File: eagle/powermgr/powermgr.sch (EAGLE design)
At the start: 18 parts, among them IC1 PIC16F1455, IC2 4027D, IC3 MCP1703DB, Q1 BSS123, Q2 BSS123, X1 MINI-USB-32005-201

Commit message: First pass of power management board completed
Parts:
- added C10, C9: .1u, resistor:C-EUC0603K
- added C11, C8: 10n, resistor:C-EUC0603K
- added C7: 0.1u, resistor:C-USC1206K
- added IC4: ACS756, custom:ACS756
- added JP5: (no value), pinhead:PINHD-1X2
- added JP6: (no value), pinhead:PINHD-1X6
- added R3: 1k, resistor:R-US_R0603
- added R4: 50k, resistor:R-US_R0603
- added R5, R6: 10k, resistor:R-US_R0603
- added R7: 220, resistor:R-US_R0603
- added X2: (no value), con-wago-500:W237-4
- C3: value (none) -> 47u; device resistor:C-EUC0805 -> resistor:CPOL-USE2.5-6
- C4, C5: value (none) -> .1u
- C6: value (none) -> 1u
- IC1: value PIC16F1455 -> PIC16F1455TSSOP-14; device custom:PIC16F1455 -> custom:PIC16F1455TSSOP-14
- IC3: value MCP1703DB -> MCP1804
- X1: value MINI-USB-32005-201 -> 10104111-0001LF; device con-cypressindustries:MINI-USB-32005-201 -> custom:10104111-0001LF
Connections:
- new net CURRENT: C8.1, IC1.RC3, R3.2
- new net N$10: C11.1, IC1.RC2, R4.1, R5.2
- new net N$11: JP6.1, R6.2, R7.2
- new net N$5: IC4.IP+, X2-1.KL, X2-2.KL
- new net N$6: IC4.IP-, X2-3.KL, X2-4.KL
- new net N$9: IC4.VOUT, R3.1
- net !MCLR: now also R7.1
- net +24V: now also C3.+, JP5.1, R4.2; no longer C3.2
- net +5V: now also C10.2, C7.1, C9.1, IC4.VCC, JP6.2, R6.1; no longer X1.1
- net GND: now also C10.1, C11.2, C3.-, C7.2, C8.2, C9.2, IC4.GND, JP5.2, JP6.3, R5.1, X1.GND; no longer C3.1, X1.5
- net ICSPCLK: now also JP6.5
- net ICSPDAT: now also JP6.4
- net USBD+: now also X1.D+; no longer X1.3
- net USBD-: now also X1.D-; no longer X1.2
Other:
- moved on the sheet: C4, C5, C6, IC3

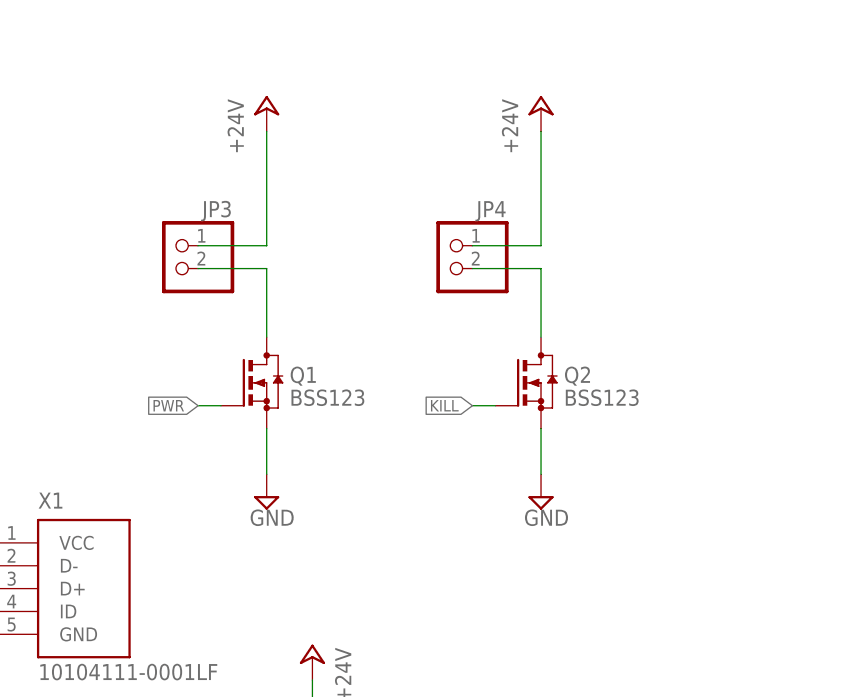
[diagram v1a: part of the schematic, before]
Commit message: Added LEDs, finalized silkscreen
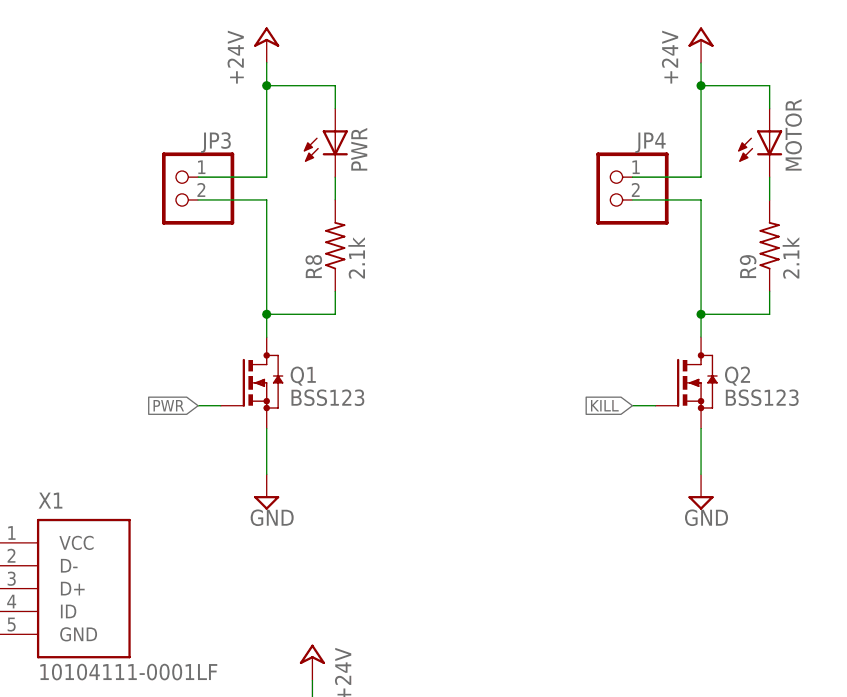
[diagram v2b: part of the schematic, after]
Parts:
- added MOTOR, PWR: (no value), led:LEDCHIP-LED0805
- added R8, R9: 2.1k, resistor:R-US_R0805
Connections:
- new net N$12: MOTOR.C, R9.2
- new net N$7: PWR.C, R8.2
- net +24V: now also MOTOR.A, PWR.A
- net N$3: now also R8.1
- net N$4: now also R9.1
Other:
- moved on the sheet: JP3, JP4, Q2
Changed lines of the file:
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@@
 <part name="SUPPLY11" library="supply2" deviceset="GND" device=""/>
 <part name="C11" library="resistor" deviceset="C-EU" device="C0603K" value="10n"/>
+<part name="R8" library="resistor" deviceset="R-US_" device="R0805" value="2.1k"/>
+<part name="R9" library="resistor" deviceset="R-US_" device="R0805" value="2.1k"/>
+<part name="PWR" library="led" deviceset="LED" device="CHIP-LED0805"/>
+<part name="MOTOR" library="led" deviceset="LED" device="CHIP-LED0805"/>
 </parts>
 <sheets>
@@
 <instance part="C2" gate="G$1" x="-86.36" y="27.94"/>
 <instance part="Q1" gate="G$1" x="134.62" y="78.74"/>
-<instance part="Q2" gate="G$1" x="165.1" y="78.74"/>
-<instance part="JP3" gate="G$1" x="124.46" y="91.44" rot="MR0"/>
-<instance part="JP4" gate="G$1" x="154.94" y="91.44" rot="MR0"/>
+<instance part="Q2" gate="G$1" x="182.88" y="78.74"/>
+<instance part="JP3" gate="G$1" x="124.46" y="99.06" rot="MR0"/>
+<instance part="JP4" gate="G$1" x="172.72" y="99.06" rot="MR0"/>
 <instance part="SUPPLY4" gate="GND" x="134.62" y="66.04"/>
-<instance part="SUPPLY5" gate="GND" x="165.1" y="66.04"/>
-<instance part="P+4" gate="1" x="134.62" y="109.22"/>
-<instance part="P+5" gate="1" x="165.1" y="109.22"/>
+<instance part="SUPPLY5" gate="GND" x="182.88" y="66.04"/>
+<instance part="P+4" gate="1" x="134.62" y="116.84"/>
+<instance part="P+5" gate="1" x="182.88" y="116.84"/>
 <instance part="SUPPLY6" gate="GND" x="101.6" y="43.18"/>
 <instance part="IC3" gate="G$1" x="71.12" y="106.68"/>
@@
 <instance part="SUPPLY11" gate="GND" x="63.5" y="-25.4"/>
 <instance part="C11" gate="G$1" x="147.32" y="22.86"/>
+<instance part="R8" gate="G$1" x="142.24" y="93.98" rot="R90"/>
+<instance part="R9" gate="G$1" x="190.5" y="93.98" rot="R90"/>
+<instance part="PWR" gate="G$1" x="142.24" y="106.68"/>
+<instance part="MOTOR" gate="G$1" x="190.5" y="106.68"/>
 </instances>
 <busses>
@@
 <pinref part="Q2" gate="G$1" pin="S"/>
 <pinref part="SUPPLY5" gate="GND" pin="GND"/>
-<wire x1="165.1" y1="73.66" x2="165.1" y2="68.58" width="0.1524" layer="91"/>
+<wire x1="182.88" y1="73.66" x2="182.88" y2="68.58" width="0.1524" layer="91"/>
 </segment>
 <segment>
@@
 <segment>
 <pinref part="Q2" gate="G$1" pin="G"/>
-<wire x1="160.02" y1="76.2" x2="157.48" y2="76.2" width="0.1524" layer="91"/>
-<label x="157.48" y="76.2" size="1.27" layer="95" rot="R180" xref="yes"/>
+<wire x1="177.8" y1="76.2" x2="175.26" y2="76.2" width="0.1524" layer="91"/>
+<label x="175.26" y="76.2" size="1.27" layer="95" rot="R180" xref="yes"/>
 </segment>
 </net>
@@
 <pinref part="Q1" gate="G$1" pin="D"/>
 <pinref part="JP3" gate="G$1" pin="2"/>
-<wire x1="134.62" y1="83.82" x2="134.62" y2="91.44" width="0.1524" layer="91"/>
-<wire x1="134.62" y1="91.44" x2="127" y2="91.44" width="0.1524" layer="91"/>
+<wire x1="134.62" y1="83.82" x2="134.62" y2="86.36" width="0.1524" layer="91"/>
+<wire x1="134.62" y1="86.36" x2="134.62" y2="99.06" width="0.1524" layer="91"/>
+<wire x1="134.62" y1="99.06" x2="127" y2="99.06" width="0.1524" layer="91"/>
+<pinref part="R8" gate="G$1" pin="1"/>
+<wire x1="142.24" y1="88.9" x2="142.24" y2="86.36" width="0.1524" layer="91"/>
+<wire x1="142.24" y1="86.36" x2="134.62" y2="86.36" width="0.1524" layer="91"/>
+<junction x="134.62" y="86.36"/>
 </segment>
 </net>
@@
 <pinref part="Q2" gate="G$1" pin="D"/>
 <pinref part="JP4" gate="G$1" pin="2"/>
-<wire x1="165.1" y1="83.82" x2="165.1" y2="91.44" width="0.1524" layer="91"/>
-<wire x1="165.1" y1="91.44" x2="157.48" y2="91.44" width="0.1524" layer="91"/>
+<wire x1="182.88" y1="83.82" x2="182.88" y2="86.36" width="0.1524" layer="91"/>
+<wire x1="182.88" y1="86.36" x2="182.88" y2="99.06" width="0.1524" layer="91"/>
+<wire x1="182.88" y1="99.06" x2="175.26" y2="99.06" width="0.1524" layer="91"/>
+<pinref part="R9" gate="G$1" pin="1"/>
+<wire x1="190.5" y1="88.9" x2="190.5" y2="86.36" width="0.1524" layer="91"/>
+<wire x1="190.5" y1="86.36" x2="182.88" y2="86.36" width="0.1524" layer="91"/>
+<junction x="182.88" y="86.36"/>
 </segment>
 </net>
@@
 <segment>
 <pinref part="JP3" gate="G$1" pin="1"/>
-<wire x1="127" y1="93.98" x2="134.62" y2="93.98" width="0.1524" layer="91"/>
-<wire x1="134.62" y1="93.98" x2="134.62" y2="106.68" width="0.1524" layer="91"/>
+<wire x1="127" y1="101.6" x2="134.62" y2="101.6" width="0.1524" layer="91"/>
+<wire x1="134.62" y1="101.6" x2="134.62" y2="111.76" width="0.1524" layer="91"/>
 <pinref part="P+4" gate="1" pin="+24V"/>
+<wire x1="134.62" y1="111.76" x2="134.62" y2="114.3" width="0.1524" layer="91"/>
+<wire x1="134.62" y1="111.76" x2="142.24" y2="111.76" width="0.1524" layer="91"/>
+<junction x="134.62" y="111.76"/>
+<pinref part="PWR" gate="G$1" pin="A"/>
+<wire x1="142.24" y1="111.76" x2="142.24" y2="109.22" width="0.1524" layer="91"/>
 </segment>
 <segment>
 <pinref part="JP4" gate="G$1" pin="1"/>
-<wire x1="157.48" y1="93.98" x2="165.1" y2="93.98" width="0.1524" layer="91"/>
-<wire x1="165.1" y1="93.98" x2="165.1" y2="106.68" width="0.1524" layer="91"/>
+<wire x1="175.26" y1="101.6" x2="182.88" y2="101.6" width="0.1524" layer="91"/>
+<wire x1="182.88" y1="101.6" x2="182.88" y2="111.76" width="0.1524" layer="91"/>
 <pinref part="P+5" gate="1" pin="+24V"/>
+<wire x1="182.88" y1="111.76" x2="182.88" y2="114.3" width="0.1524" layer="91"/>
+<wire x1="182.88" y1="111.76" x2="190.5" y2="111.76" width="0.1524" layer="91"/>
+<junction x="182.88" y="111.76"/>
+<pinref part="MOTOR" gate="G$1" pin="A"/>
+<wire x1="190.5" y1="111.76" x2="190.5" y2="109.22" width="0.1524" layer="91"/>
 </segment>
 <segment>
@@
 </segment>
 </net>
+<net name="N$7" class="0">
+<segment>
+<pinref part="PWR" gate="G$1" pin="C"/>
+<pinref part="R8" gate="G$1" pin="2"/>
+<wire x1="142.24" y1="101.6" x2="142.24" y2="99.06" width="0.1524" layer="91"/>
+</segment>
+</net>
+<net name="N$12" class="0">
+<segment>
+<pinref part="MOTOR" gate="G$1" pin="C"/>
+<pinref part="R9" gate="G$1" pin="2"/>
+<wire x1="190.5" y1="101.6" x2="190.5" y2="99.06" width="0.1524" layer="91"/>
+</segment>
+</net>
